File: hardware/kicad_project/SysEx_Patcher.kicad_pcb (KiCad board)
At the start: 4 copper layers, 172 x 228 mm, 86 parts, among them J1 MIDI_IN, J10 JACK6.35, J2 MIDI_OUT, J3 DC_5V, J4 BAT_PWR, J5 OLED, SW1 prog/MIDI, SW2 SW, SW3 SW, SW4 SW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

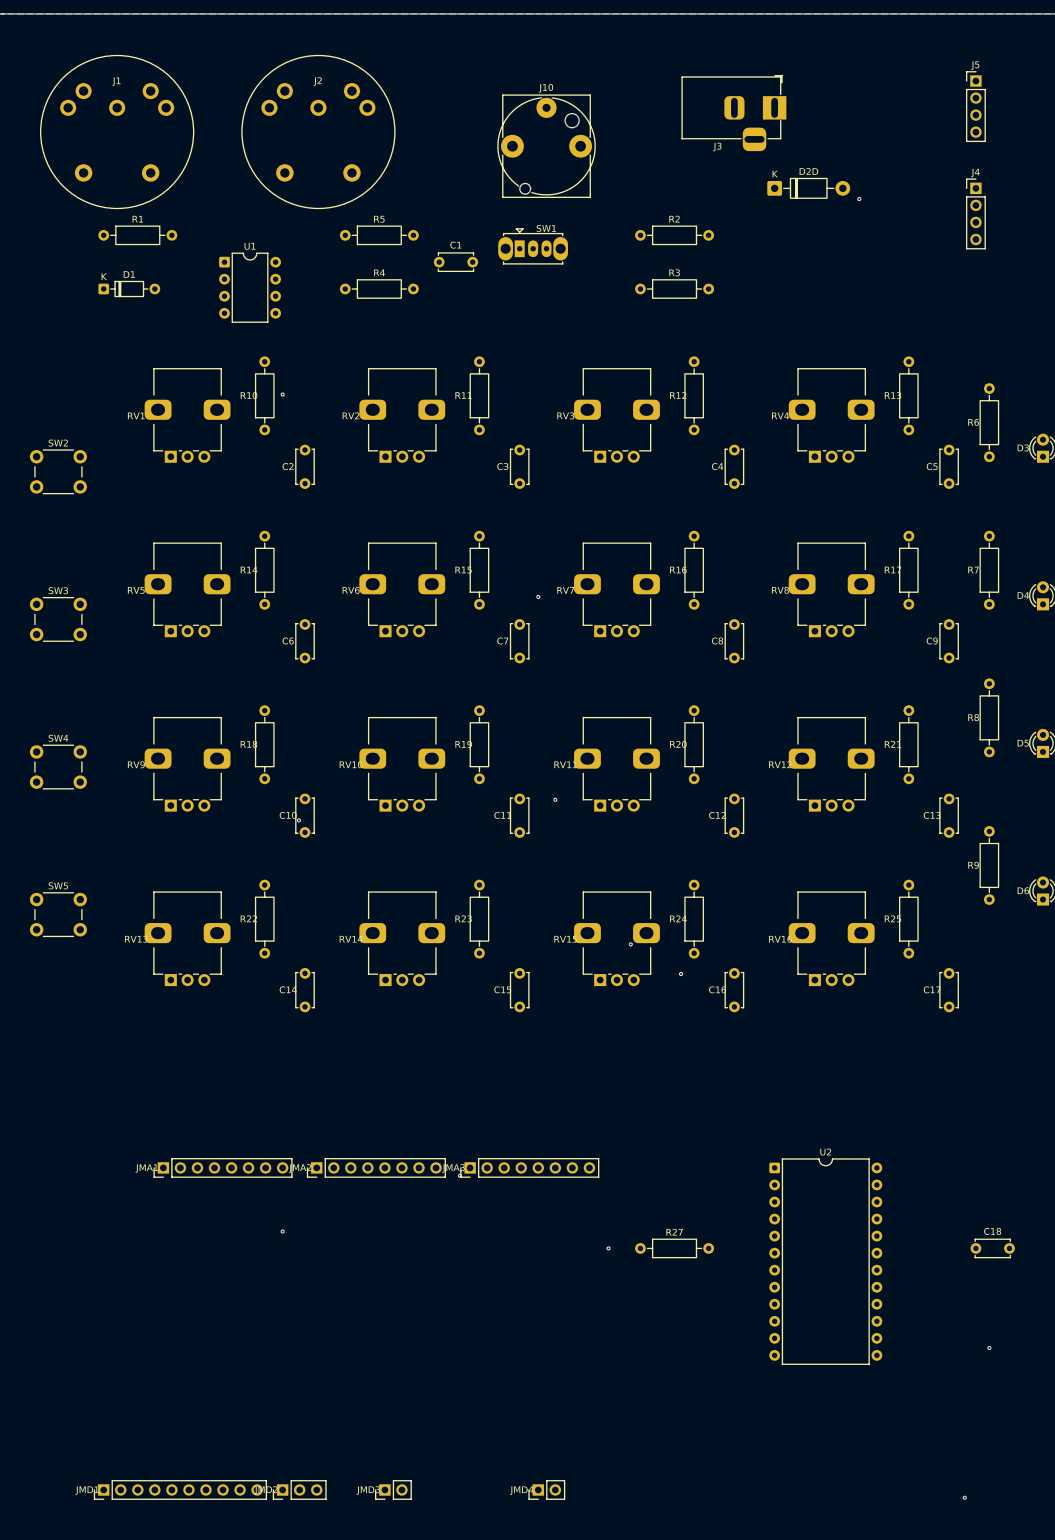
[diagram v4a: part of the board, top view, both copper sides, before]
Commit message: hardware: fix connector orientations + horizontal jack, reroute clean
- MIDI DIN-5 (J1/J2): rebuild footprint to match original PCB orientation
  (mount holes at top, signal arc below, data pins 4/5 lowest) — was upside down
- 6.35mm jack (J10): switch to Neutrik NRJ6HF-1 horizontal, nose toward the top
  edge so the cable plugs in horizontally from the top (was vertical NJ3FD-V)
- DC barrel (J3): rotate 270deg so the opening faces the top edge like the
  other inputs (was facing left)
- OLED (J5): plain 1x4 header, no pin-name silkscreen
- move 4067 mux + jack RC filter into the gap between the two Mega header rows
  to declutter the dense analog header row (fixes autorouter A15/D10 shorts)
- full reroute: 0 unconnected, DRC clean; regenerate fab Gerbers + previews
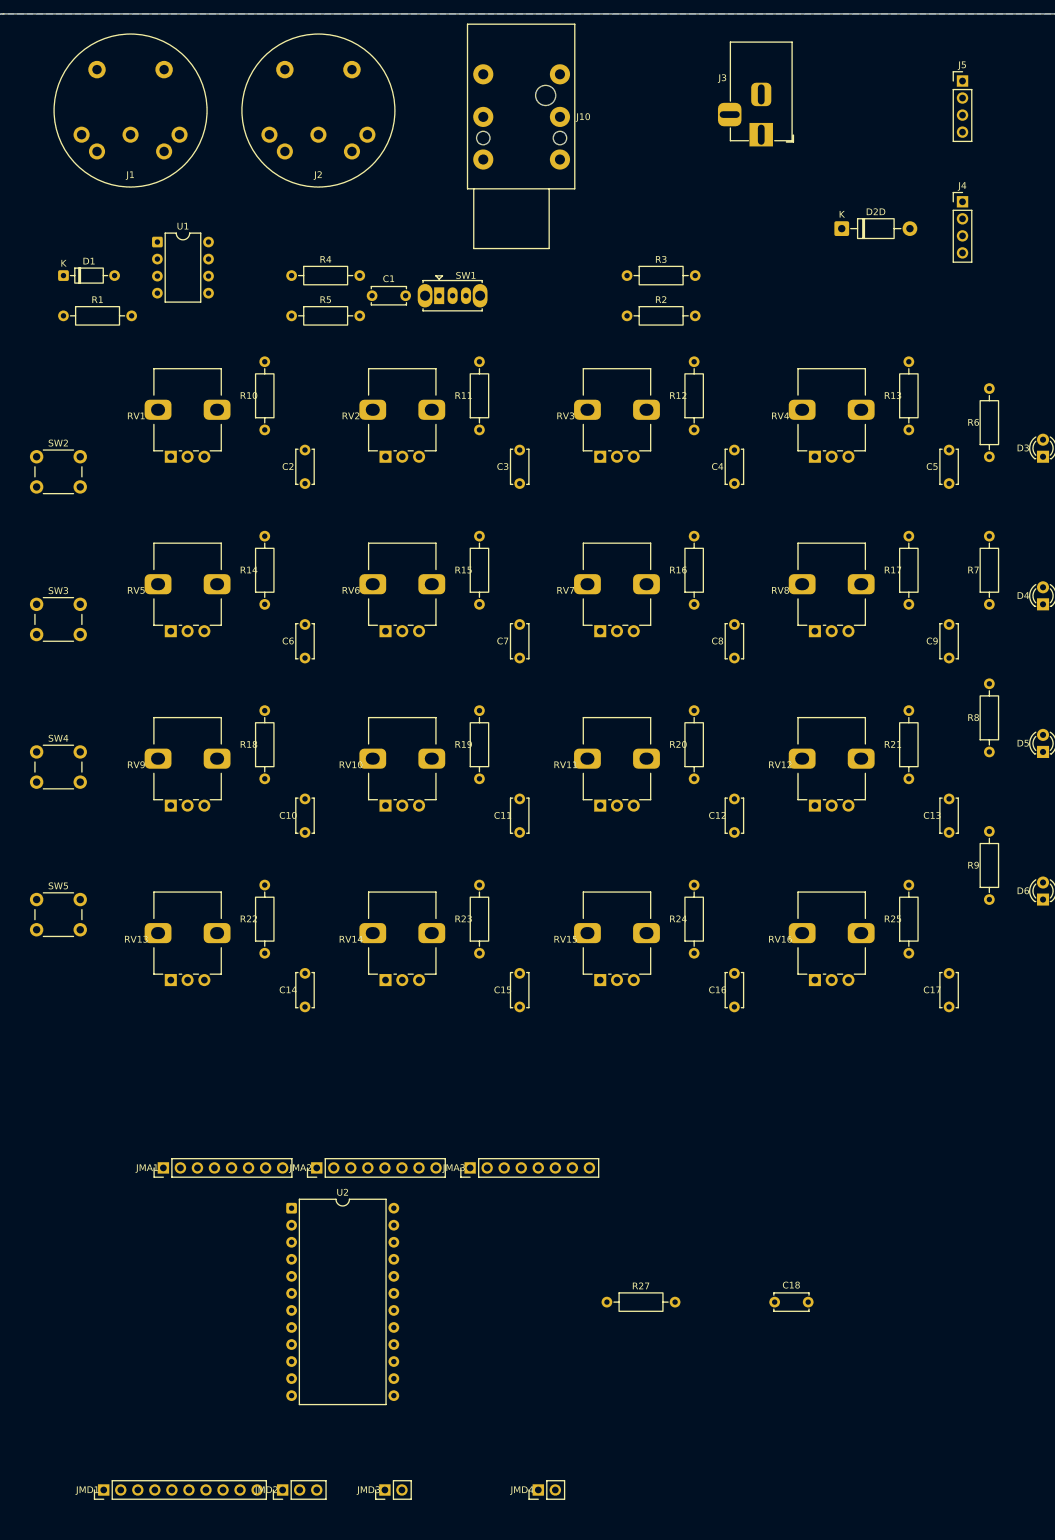
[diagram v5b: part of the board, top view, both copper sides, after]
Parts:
- J10: footprint Connector_Audio:Jack_6.35mm_Neutrik_NJ3FD-V_Vertical -> Connector_Audio:Jack_6.35mm_Neutrik_NRJ6HF-1_Horizontal
- moved U2 72.2 mm to (48.0, 178.0)
- moved C18 31.0 mm to (120.0, 192.0)
- moved R5 14.4 mm to (48.0, 45.0)
- moved SW1 13.9 mm to (70.0, 42.0)
- moved R1 13.4 mm to (14.0, 45.0)
- moved R2 12.2 mm to (98.0, 45.0)
- moved D2D 11.7 mm to (130.0, 32.0)
- moved C1 11.2 mm to (60.0, 42.0)
- moved U1 10.4 mm to (28.0, 34.0)
- moved R27 9.43 mm to (95.0, 192.0)
- moved R4 8.25 mm to (48.0, 39.0)
- moved D1 6.32 mm to (14.0, 39.0)
- moved J10 5.39 mm to (88.0, 9.00), turned to 270 degrees
- moved J1 4.47 mm to (24.0, 18.0)
- moved J3 4.47 mm to (118.0, 18.0), turned to 270 degrees
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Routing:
- net +5V: track 672.4 -> 0.00 mm, vias 1 -> 0
- net D12: track 253.7 -> 0.00 mm, vias 1 -> 0
- net VIN_RAW: track 250.8 -> 0.00 mm, vias 1 -> 0
- net D21_SCL: track 231.9 -> 0.00 mm
- net D20_SDA: track 229.4 -> 0.00 mm
- net D11: track 221.8 -> 0.00 mm, vias 1 -> 0
- net D1_TX: track 202.6 -> 0.00 mm
- net D0_RX: track 193.1 -> 0.00 mm
- net D9: track 186.4 -> 0.00 mm, vias 1 -> 0
- net JACK_W: track 178.6 -> 0.00 mm, vias 1 -> 0
- net D10: track 176.2 -> 0.00 mm, vias 1 -> 0
- net D7: track 175.8 -> 0.00 mm
- net A12: track 174.9 -> 0.00 mm, vias 1 -> 0
- net D8: track 148.4 -> 0.00 mm
- net A13: track 143.0 -> 0.00 mm, vias 1 -> 0
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
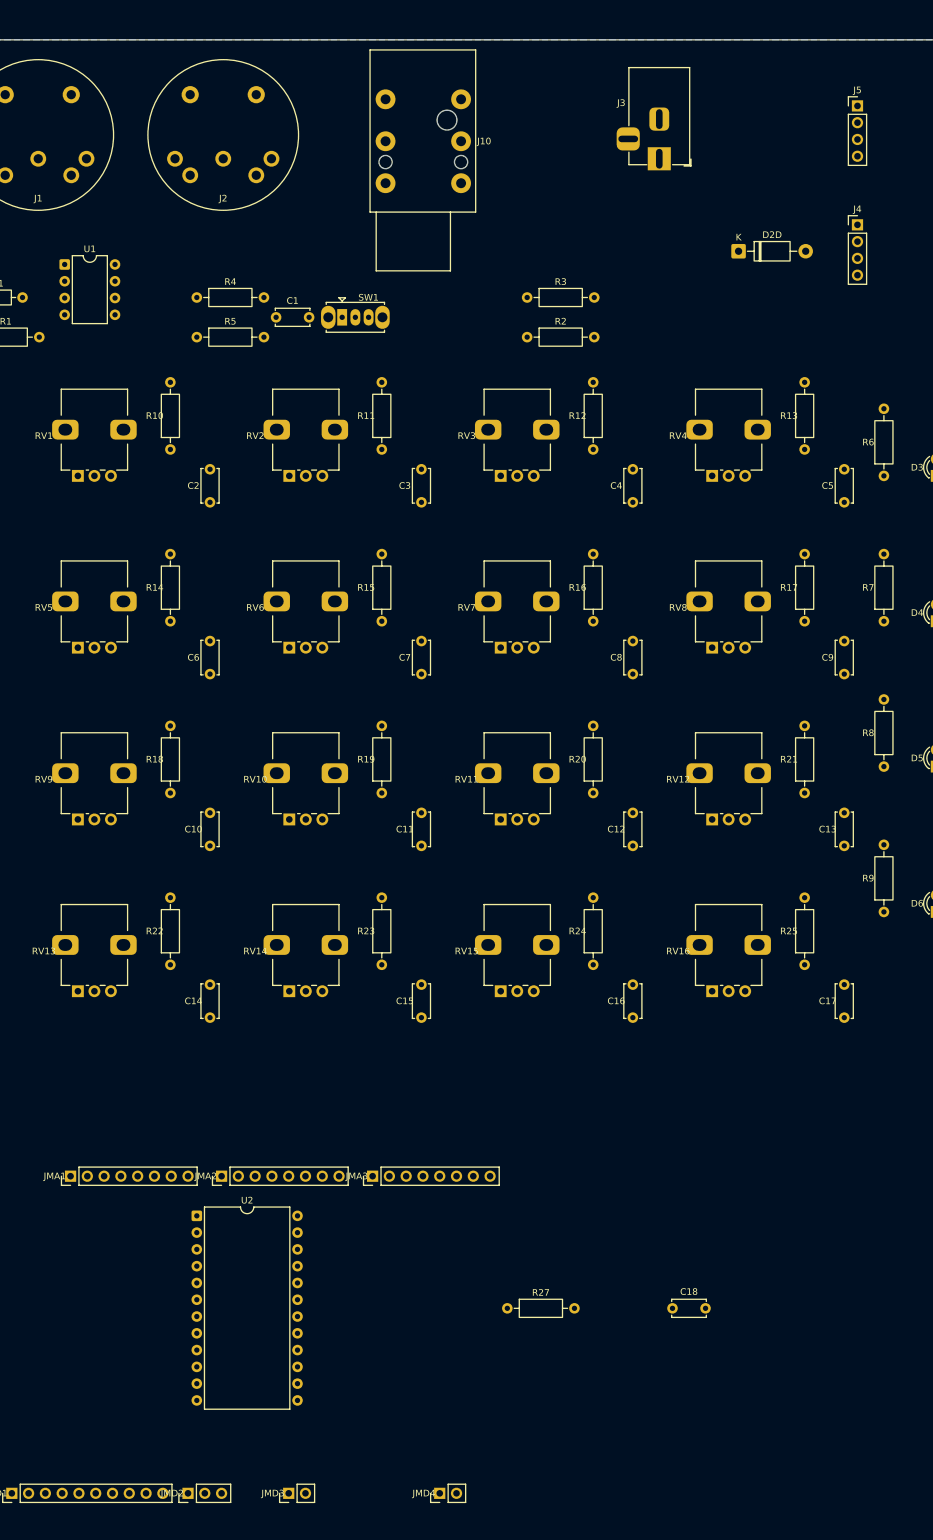
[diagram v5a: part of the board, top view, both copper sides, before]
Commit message: hardware: fix 6.35mm jack orientation (nose now faces the top edge)
The NRJ6HF-1 opening is on the footprint +x side (Sleeve pad nearest the
opening, Tip deepest). The previous 270deg rotation pointed the threaded nose
DOWN into the board; rotate to 90deg so the nose protrudes past the TOP edge and
the cable plugs in horizontally from the top. Reroute: 0 unconnected, DRC clean;
regenerate fab Gerbers + previews.
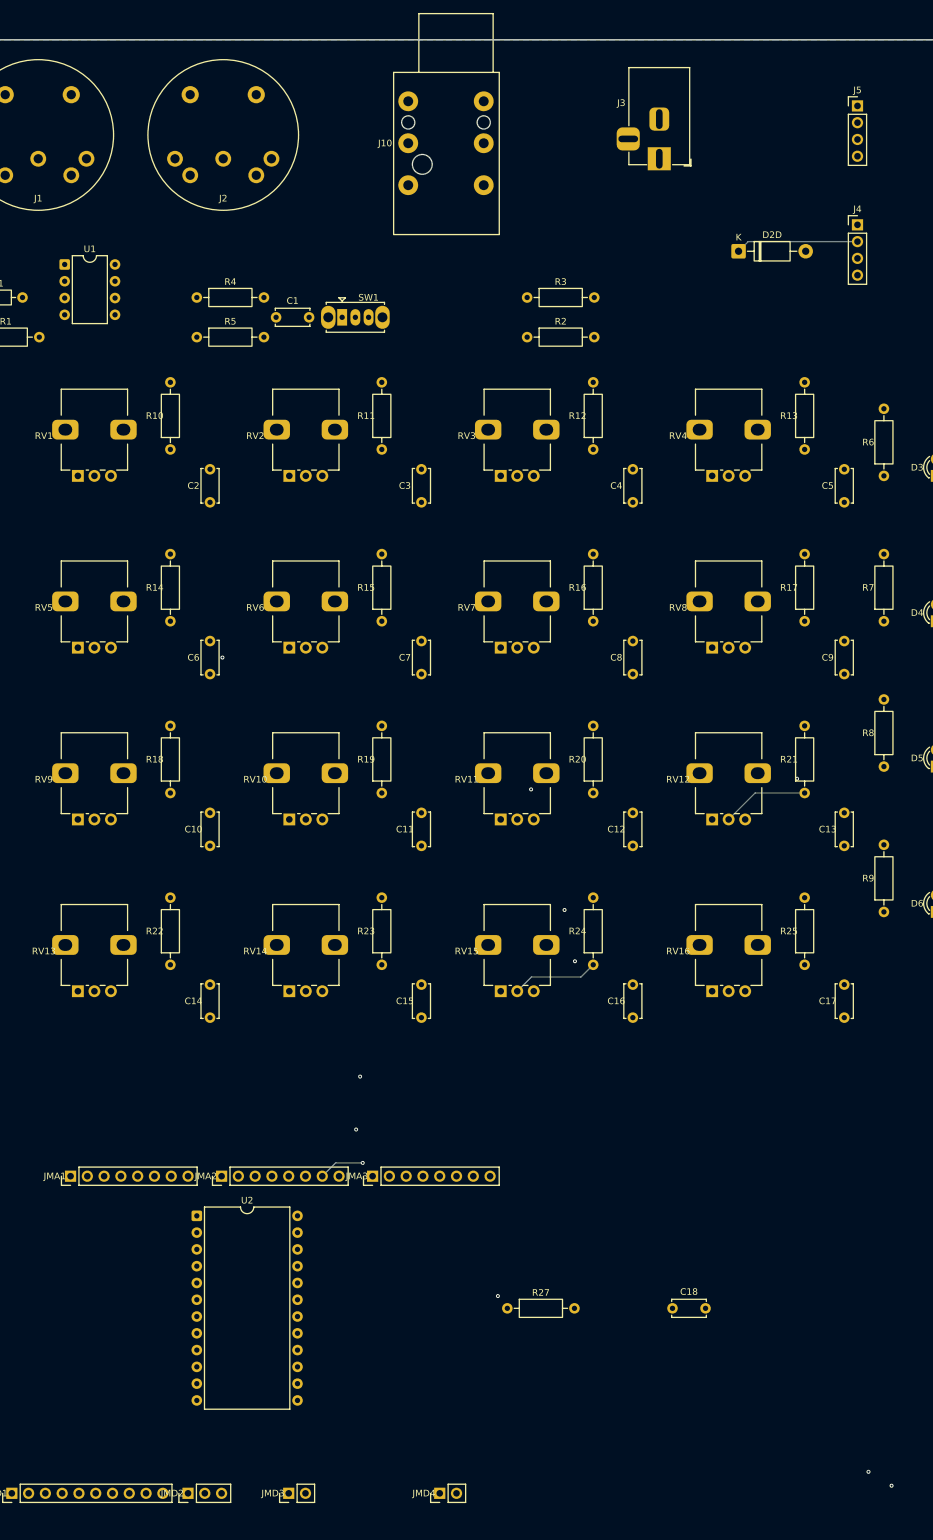
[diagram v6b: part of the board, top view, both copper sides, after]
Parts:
- moved J10 15.3 mm to (80.0, 22.0), turned to 90 degrees
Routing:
- net +5V: track 0.00 -> 666.3 mm
- net D12: track 0.00 -> 255.2 mm, vias 0 -> 1
- net D20_SDA: track 0.00 -> 237.5 mm
- net D11: track 0.00 -> 237.2 mm, vias 0 -> 1
- net D21_SCL: track 0.00 -> 230.1 mm
- net VIN_RAW: track 0.00 -> 222.2 mm, vias 0 -> 1
- net D10: track 0.00 -> 212.2 mm, vias 0 -> 1
- net D1_TX: track 0.00 -> 203.8 mm
- net D0_RX: track 0.00 -> 181.1 mm
- net JACK_W: track 0.00 -> 176.2 mm, vias 0 -> 1
- net D7: track 0.00 -> 169.3 mm
- net D9: track 0.00 -> 162.9 mm
- net D8: track 0.00 -> 151.8 mm
- net A12: track 0.00 -> 148.2 mm, vias 0 -> 1
- net MUX_CH0: track 0.00 -> 144.3 mm
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
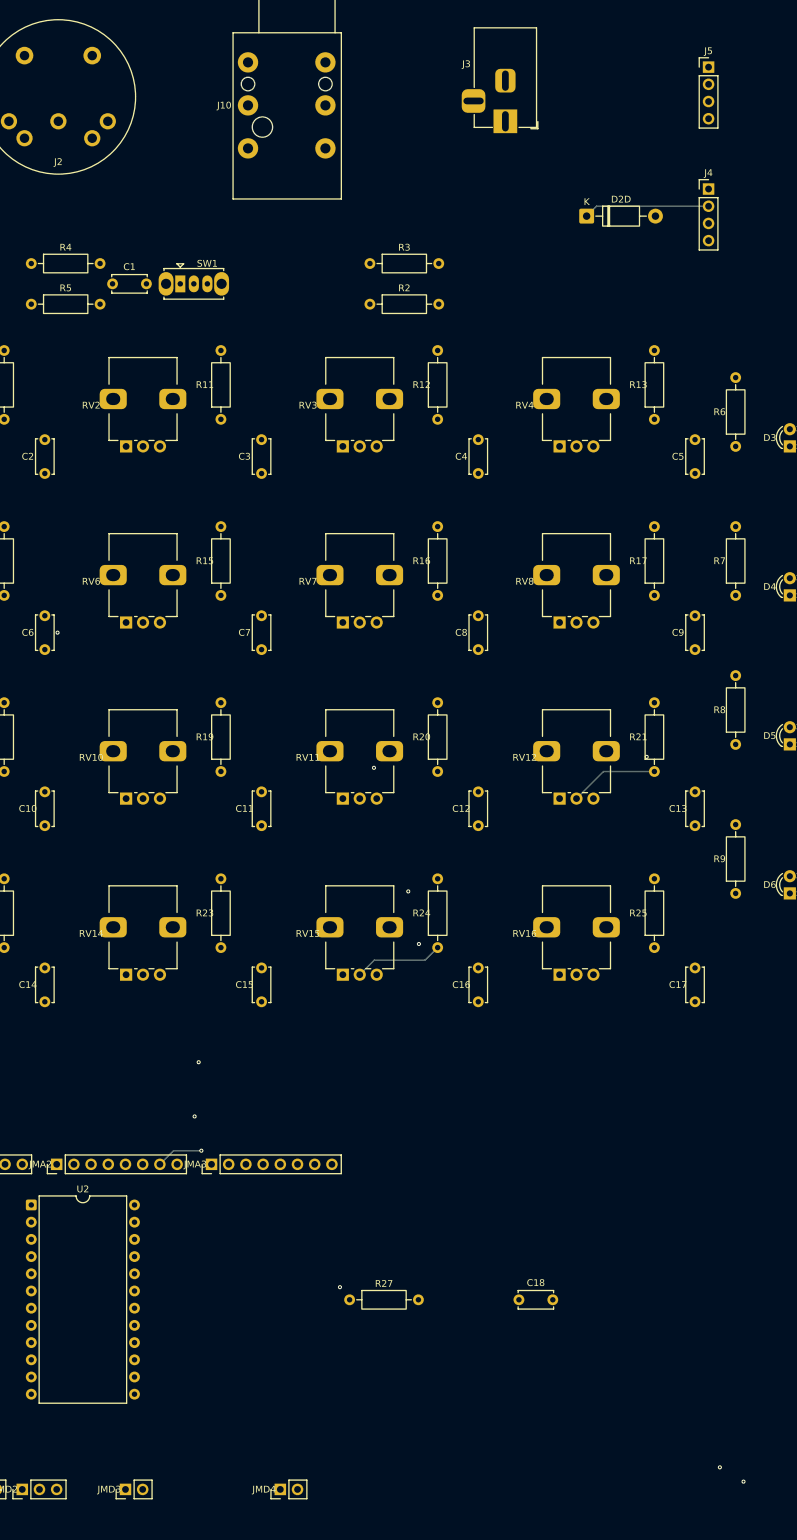
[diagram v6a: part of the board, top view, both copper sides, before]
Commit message: hardware: OLED header J5 rotated 90deg + silkscreen pin labels (GND/VCC/SCL/SDA)
J5 now sits as a horizontal 1x4 row with each pin labelled on the silkscreen
(GND, VCC, SCL, SDA) above its pad. Reroute: 0 unconnected, DRC clean;
regenerate fab Gerbers + previews.
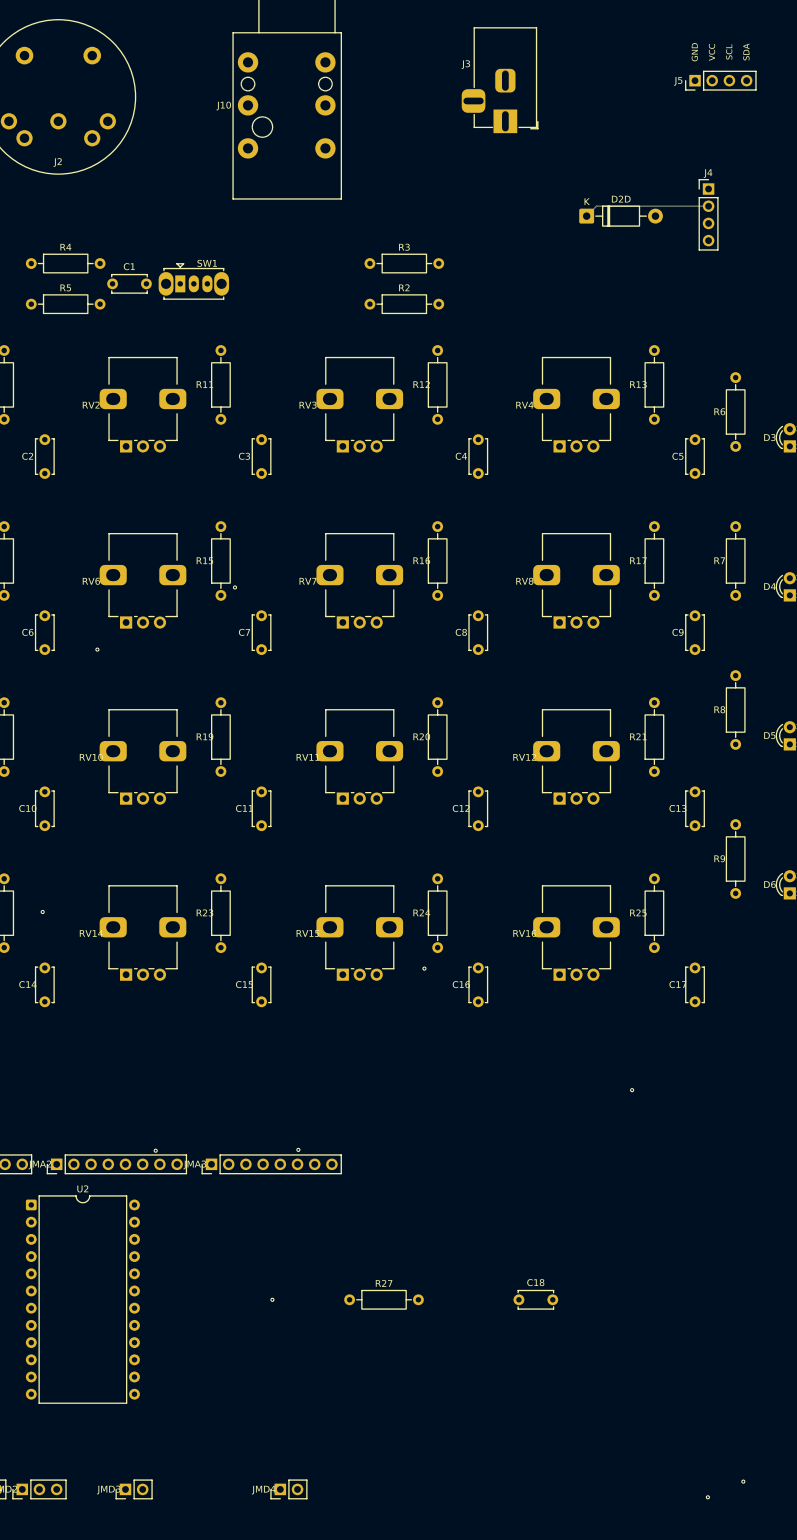
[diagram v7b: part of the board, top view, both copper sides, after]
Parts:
- moved J5 2.83 mm to (146.0, 12.0), turned to 90 degrees
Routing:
- net A12: track 148.2 -> 174.8 mm
- net VIN_RAW: track 222.2 -> 244.9 mm
- net D11: track 237.2 -> 214.7 mm
- net A4: track 105.2 -> 122.6 mm
- net A8: track 140.0 -> 152.3 mm
- net +5V: track 666.3 -> 675.5 mm
- net JACK_W: track 176.2 -> 182.9 mm
- net D20_SDA: track 237.5 -> 242.3 mm
- net D21_SCL: track 230.1 -> 234.4 mm
- net D10: track 212.2 -> 216.1 mm
- net MUX_CH0: track 144.3 -> 147.1 mm
- net A6: track 79.3 -> 76.9 mm, vias 1 -> 0
- net A11: track 63.8 -> 65.2 mm
- net A13: track 121.0 -> 121.9 mm
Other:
- board text added: "GND"
- board text added: "SCL"
- board text added: "SDA"
- board text added: "VCC"
